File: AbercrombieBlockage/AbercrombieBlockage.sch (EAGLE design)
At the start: 32 parts, among them U1 CY8CKIT-142, U2 DMN3135LVT, U3 DMN3135LVT, U4 DMN3135LVT, U5 M95M01

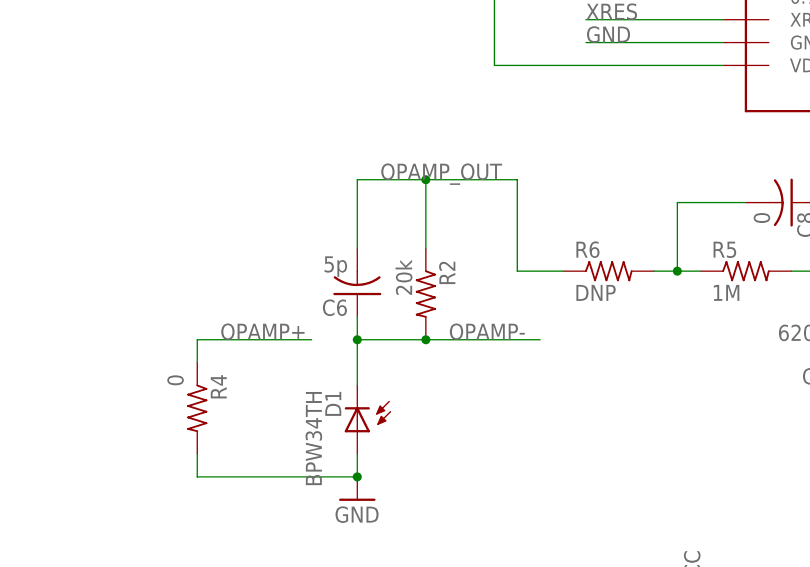
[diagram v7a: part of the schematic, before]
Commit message: Added a readme indicated the Abercrombie projects have been moved.
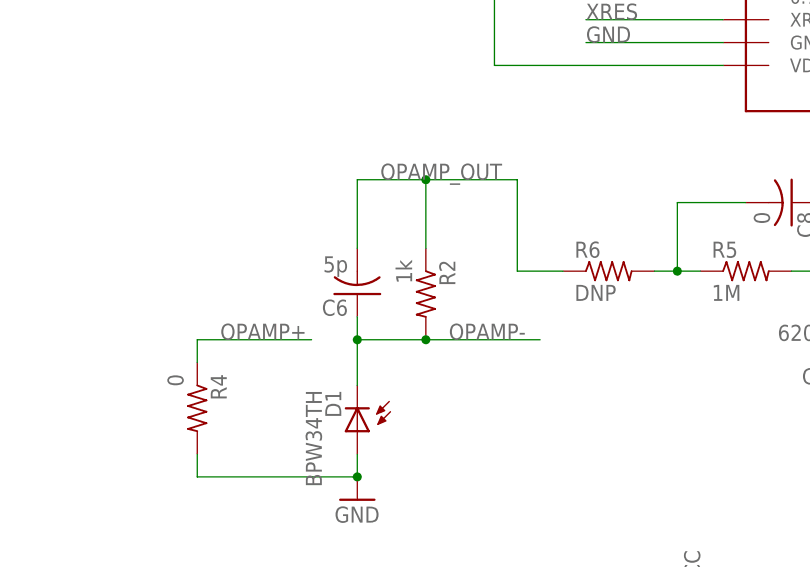
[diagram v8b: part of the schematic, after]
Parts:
- R2: value 20k -> 1k
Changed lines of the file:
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@@
 <part name="C5" library="resistor" deviceset="C-US" device="C0603" value="1u"/>
 <part name="C6" library="resistor" deviceset="C-US" device="C0603" value="5p"/>
-<part name="R2" library="resistor" deviceset="R-US_" device="R0603" value="20k"/>
+<part name="R2" library="resistor" deviceset="R-US_" device="R0603" value="1k"/>
 <part name="D1" library="NicksParts" deviceset="BPW34" device="" technology="TH"/>
 <part name="GND6" library="supply1" deviceset="GND" device=""/>
